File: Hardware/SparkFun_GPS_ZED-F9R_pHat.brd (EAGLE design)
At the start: 65 x 57.3 mm, 121 parts, among them J1 U.FL, J5 QWIIC_RIGHT_ANGLE, J6 RASPBERRYPI-40-PIN-GPIO_SMD_S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, U1 UBLOX_ZED_F9R, U2 HCPL-073L, U3 UHS_INVERTER_SCHMITT_TRIGGERS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, U4 UHS_INVERTER_SCHMITT_TRIGGERS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

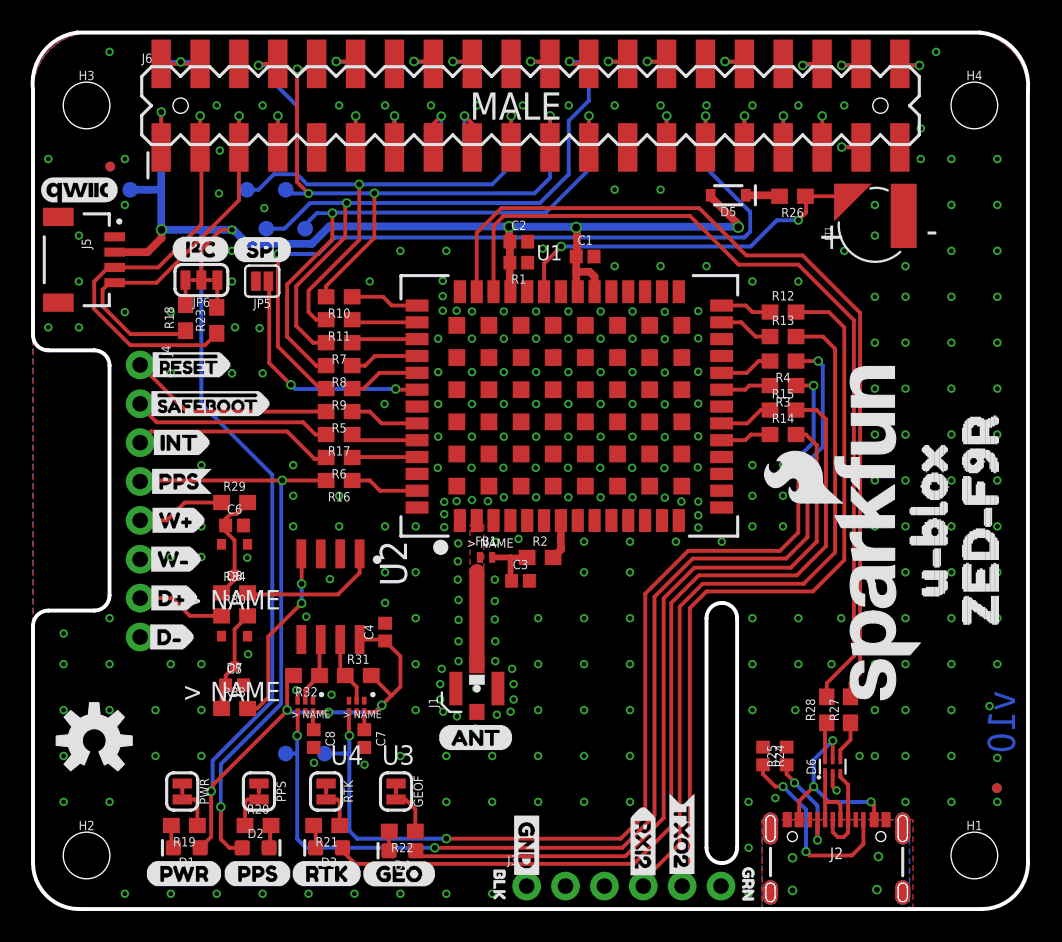
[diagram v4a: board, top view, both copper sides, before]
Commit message: Adds 33 Ohm resistor arrays and custom silk
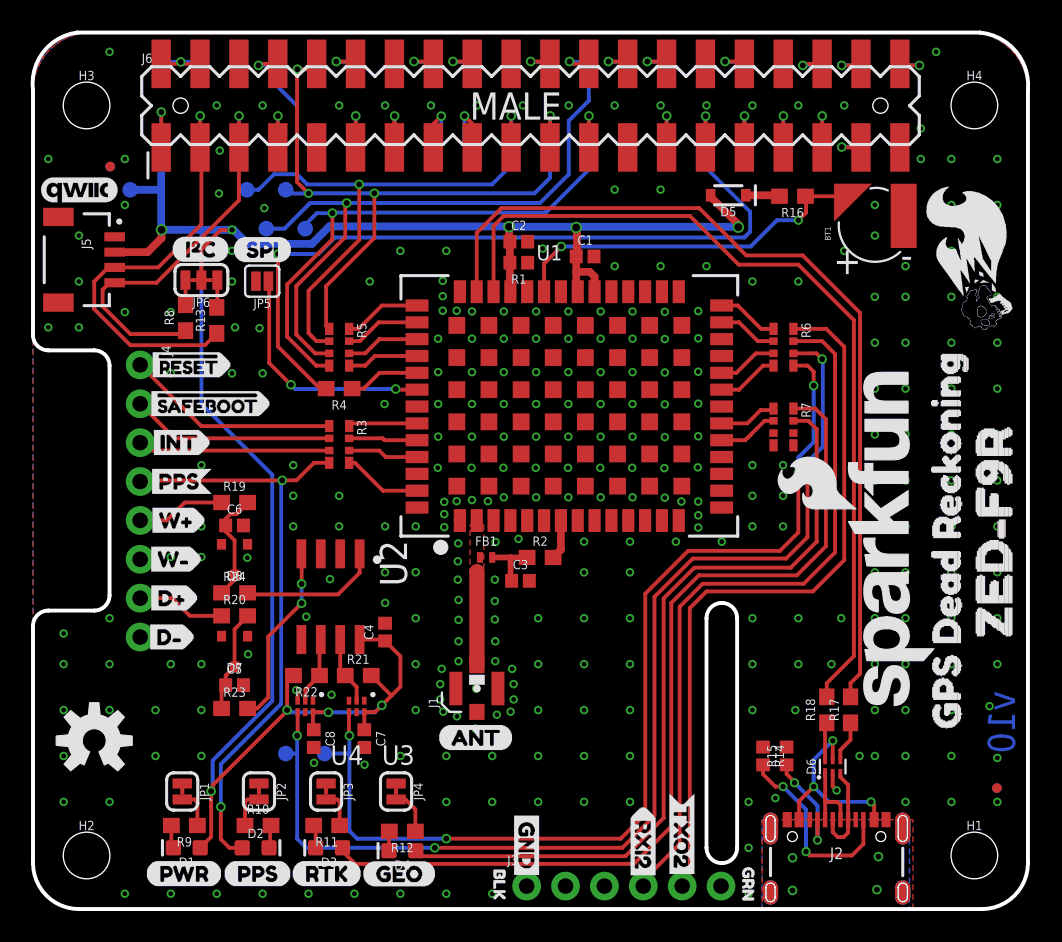
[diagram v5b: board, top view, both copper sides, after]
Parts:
- removed R25: 5.1k, SparkFun-Resistors:0402
- removed R26, R29, R30: 3.3k, SparkFun-Resistors:0603
- removed R27, R28: 27, SparkFun-Resistors:0603
- removed R31, R32: 910, classified:0603
- removed R33, R34: 470, SparkFun-Resistors:0603
- added U$31: (no value), Dead#Reckoning#GPS#board#silk#FINALSMALL:DEAD#RECKONING#GPS#BOARD#SILK#FINAL#PNG
- added U$36: (no value), Dead#Reckoning#GPS#board#silk#FINAL#png:DEAD#RECKONING#GPS#BOARD#SILK#FINAL#PNG
- R10, R11, R12, R9: value 33 -> 1k
- R13, R8: value 33 -> 2.2k
- R14, R15: value 33 -> 5.1k; device SparkFun-Resistors:0603 -> SparkFun-Resistors:0402
- R16: value 33 -> 3.3k
- R17: value 33 -> 27
- R18: value 2.2k -> 27
- R19, R20: value 1k -> 3.3k
- R21, R22: value 1k -> 910; device SparkFun-Resistors:0603 -> classified:0603
- R23: value 2.2k -> 470
- R24: value 5.1k -> 470; device SparkFun-Resistors:0402 -> SparkFun-Resistors:0603
- R3, R5, R6, R7: device SparkFun-Resistors:0603 -> SparkFun-Resistors:1206_RA
- U$25: device zed:U#BLOX1 -> Dead Reckoning:GPS_DEAD_RECKONING0
- moved R18 49.1 mm to (51.9, 13.0)
- moved R12 42.1 mm to (24.1, 5.08), turned to 180 degrees
- moved R17 37.9 mm to (53.4, 13.0), turned to 90 degrees
- moved R13 37.0 mm to (12.0, 38.5), turned to 90 degrees
- moved R24 36.1 mm to (13.2, 20.7), turned to 0 degrees
- moved R16 35.0 mm to (49.6, 46.6)
- moved R10 34.9 mm to (14.7, 5.46), turned to 0 degrees
- moved R11 33.1 mm to (19.2, 5.46)
- moved R9 30.3 mm to (9.89, 5.46)
- moved R6 29.9 mm to (49.0, 36.7), turned to 270 degrees
- moved R7 29.5 mm to (49.0, 31.5), turned to 270 degrees
- moved R3 29.3 mm to (20.0, 30.4), turned to 270 degrees
- moved R4 29.1 mm to (20.0, 34.0)
- moved R23 25.4 mm to (13.2, 13.1), turned to 0 degrees
- moved R15 22.6 mm to (49.2, 10.0), turned to 270 degrees
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- renumbered GEOF to JP4, PPS to JP2, PWR to JP1, RTK to JP3
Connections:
- net !RESET: now also R3.P1; no longer R5.2
- net !SAFEBOOT: now also R3.P2; no longer R17.2
- net 3.3V: now also R21.2, R22.2; no longer R31.2, R32.2
- net DIR+: now also R20.1; no longer R30.1
- net DIR_IN: now also R23.2; no longer R33.2
- net DIR_OUT: now also R6.P6; no longer R4.1
- net DIR_SCHMITT: now also R22.1; no longer R32.1
- net DMINUS: now also R18.2; no longer R28.2
- net DPLUS: now also R17.2; no longer R27.2
- net GEOF_STAT: now also R7.P7; no longer R14.2
- net GND: now also R14.1, R15.1; no longer R24.1, R25.1
- net INT: now also R3.P3; no longer R6.2
- net N$1: now also R13.2; no longer R23.2
- net N$12: now also R14.2; no longer R24.2
- net N$13: now also R3.P8; no longer R5.1
- net N$14: now also R3.P6; no longer R6.1
- net N$15: now also R5.P6; no longer R7.1
- net N$16: now also R12.1; no longer R22.1
- net N$17: now also R12.2; no longer R22.2
- net N$18: now also R15.2; no longer R25.2
- net N$19: now also R5.P5; no longer R8.1
- net N$2: now also R16.2; no longer R26.2
- net N$20: now also R4.1; no longer R9.1
- net N$21: now also R5.P8; no longer R10.1
- net N$22: now also R11.1; no longer R21.1
- net N$23: now also R10.1; no longer R20.1
- net N$24: now also R10.2; no longer R20.2
- net N$25: now also R11.2; no longer R21.2
- net N$26: now also R5.P7; no longer R11.1
- net N$27: now also R19.2, R24.1; no longer R29.2, R34.1
- net N$28: now also R7.P2; no longer R14.1
- net N$29: now also R7.P1; no longer R15.1
- net N$3: now also R8.2; no longer R18.2
- net N$30: now also R3.P5; no longer R16.1
- net N$31: now also R3.P7; no longer R17.1
- net N$32: now also R6.P1; no longer R12.1
- net N$33: now also R6.P2; no longer R13.1
- net N$34: now also R6.P4; no longer R3.2
- net N$35: now also R6.P3; no longer R4.2
- net N$36: now also R20.2, R23.1; no longer R30.2, R33.1
- net N$4: now also R9.2; no longer R19.2
- net N$6: now also R18.1; no longer R28.1
- net N$7: now also R17.1; no longer R27.1
- net N$8: now also R9.1; no longer R19.1
- net PPS: now also R3.P4; no longer R16.2
- net QWIIC_SCL: now also R8.1; no longer R18.1
- net QWIIC_SDA: now also R13.1; no longer R23.1
- net RTK_STAT: now also R7.P8; no longer R15.2
- net RXI/MOSI: now also R5.P2; no longer R11.2
- net RXI2: now also R6.P7; no longer R13.2
- net SCL/CLK: now also R5.P4; no longer R8.2
- net SDA/!CS: now also R5.P3; no longer R7.2
- net TXO/MISO: now also R5.P1; no longer R10.2
- net TXO2: now also R6.P8; no longer R12.2
- net TX_READY: now also R4.2; no longer R9.2
- net V_BATT: now also R16.1; no longer R26.1
- net WT+: now also R19.1; no longer R29.1
- net WT_IN: now also R24.2; no longer R34.2
- net WT_OUT: now also R6.P5; no longer R3.1
- net WT_SCHMITT: now also R21.1; no longer R31.1
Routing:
- net TXO/MISO: track 43.4 -> 45.5 mm
- net RXI/MOSI: track 45.4 -> 47.0 mm
- net WT_OUT: track 66.8 -> 68.1 mm
- net GEOF_STAT: track 51.3 -> 52.4 mm
- net TXO2: track 48.5 -> 47.5 mm
- net SDA/!CS: track 43.5 -> 44.3 mm
- net N$34: track 3.27 -> 4.04 mm
- net INT: track 13.3 -> 12.6 mm
- net PPS: track 38.9 -> 39.6 mm
- net N$32: track 3.34 -> 4.02 mm
- net N$30: track 4.52 -> 5.19 mm
- net N$26: track 4.31 -> 4.94 mm
- net DIR_OUT: track 72.9 -> 73.5 mm
- net N$28: track 3.32 -> 3.91 mm
- net !RESET: track 13.4 -> 14.0 mm
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
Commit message: Updates all parts to parts in the Eagle Library
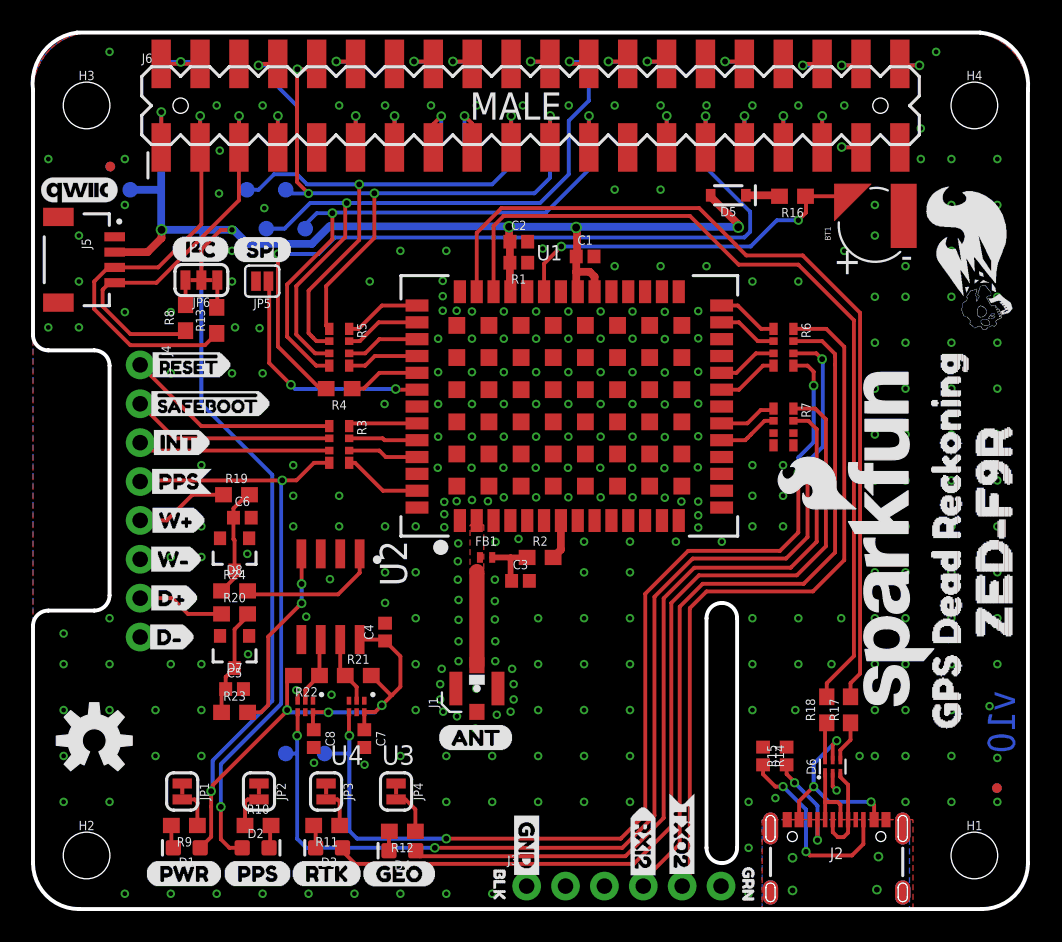
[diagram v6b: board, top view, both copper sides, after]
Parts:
- D7, D8: value 0.5A/40V/420mV -> 15V; device classified:SOT23_BZX -> SparkFun-DiscreteSemi:SOT23-3
- U1: value UBLOX_ZED_F9R -> U-BLOX_ZED_F9R; device classified:UBLOX_ZED_F9R -> SparkFun-GPS:UBLOX_ZED_F9R
- U2: value HCPL-073L -> DUAL-OPTO_HCPL-073L; device classified:SOP_8-PIN -> SparkFun-DiscreteSemi:SOP_8-PIN
- U3, U4: device classified:SIP6 -> SparkFun-IC-Amplifiers:SIP6
- moved C6 0.72 mm to (13.7, 25.6)
- moved R19 0.52 mm to (13.3, 27.1)
- moved D8 0.38 mm to (13.2, 23.2)
- moved C5 0.25 mm to (13.2, 14.4)
- moved R23 0.25 mm to (13.2, 12.8)
- moved R20 0.13 mm to (13.2, 19.3)
- moved R24 0.13 mm to (13.2, 20.8)
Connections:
- net GND: now also D7.1, D8.1; no longer D7.P1, D8.P1
- net N$27: now also D8.3; no longer D8.P3
- net N$36: now also D7.3; no longer D7.P3

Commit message: Replaces 910 Ohm resistor with part from Eagle Library
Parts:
- R21, R22: device classified:0603 -> SparkFun-Resistors:0603
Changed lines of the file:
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@@
 <attribute name="VALUE" value="15V" x="13.16745" y="23.223" size="1.778" layer="27" rot="R180" display="off"/>
 </element>
-<element name="R21" library="classified" package="0603" value="910" x="21.25" y="15.257" smashed="yes">
+<element name="R21" library="SparkFun-Resistors" package="0603" value="910" x="21.25" y="15.257" smashed="yes">
 <attribute name="NAME" x="21.25" y="16.019" size="0.6096" layer="25" font="vector" ratio="20" align="bottom-center"/>
 <attribute name="PROD_ID" value="RES-13860" x="0.25" y="17.257" size="1.778" layer="27" font="vector" ratio="15" display="off"/>
 <attribute name="VALUE" x="21.25" y="14.495" size="0.6096" layer="27" font="vector" ratio="20" align="top-center"/>
 </element>
-<element name="R22" library="classified" package="0603" value="910" x="17.866" y="15.257" smashed="yes" rot="R180">
+<element name="R22" library="SparkFun-Resistors" package="0603" value="910" x="17.866" y="15.257" smashed="yes" rot="R180">
 <attribute name="NAME" x="17.866" y="14.495" size="0.6096" layer="25" font="vector" ratio="20" rot="R180" align="bottom-center"/>
 <attribute name="PROD_ID" value="RES-13860" x="42.866" y="17.257" size="1.778" layer="27" font="vector" ratio="15" rot="R180" display="off"/>

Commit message: Updates cooool skull silk
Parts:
- U$31: device Dead#Reckoning#GPS#board#silk#FINALSMALL:DEAD#RECKONING#GPS#BOARD#SILK#FINAL#PNG -> Dead#Reckoning#GPS#board#silk#FINALSMALL:DEAD#RECKONING#GPS#BOARD#SILK#FINAL#JPG
- U$36: device Dead#Reckoning#GPS#board#silk#FINAL#png:DEAD#RECKONING#GPS#BOARD#SILK#FINAL#PNG -> Dead#Reckoning#GPS#board#silk#FINAL#png:DEAD#RECKONING#GPS#BOARD#SILK#FINAL#JPG
- moved U$36 0.85 mm to (33.9, 26.2)
- moved U$31 0.52 mm to (61.2, 42.0)
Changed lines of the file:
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@@
 <attribute name="VALUE" x="47.1963" y="33.101" size="0.6096" layer="27" rot="R270"/>
 </element>
-<element name="U$36" library="Dead#Reckoning#GPS#board#silk#FINAL#png" package="DEAD#RECKONING#GPS#BOARD#SILK#FINAL#PNG" value="" x="34.29" y="25.4" smashed="yes" rot="MR0"/>
-<element name="U$31" library="Dead#Reckoning#GPS#board#silk#FINALSMALL" package="DEAD#RECKONING#GPS#BOARD#SILK#FINAL#PNG" value="" x="61.087" y="42.545" smashed="yes" rot="R90"/>
 <element name="U$25" library="Dead Reckoning" package="GPS_DEAD_RECKONING0" value="" x="59.69" y="10.16" smashed="yes" rot="R90"/>
+<element name="U$31" library="Dead#Reckoning#GPS#board#silk#FINALSMALL" package="DEAD#RECKONING#GPS#BOARD#SILK#FINAL#JPG" value="" x="61.214" y="42.037" smashed="yes" rot="R90"/>
+<element name="U$36" library="Dead#Reckoning#GPS#board#silk#FINAL#png" package="DEAD#RECKONING#GPS#BOARD#SILK#FINAL#JPG" value="" x="33.909" y="26.162" smashed="yes" rot="MR0"/>
 </elements>
 <signals>
